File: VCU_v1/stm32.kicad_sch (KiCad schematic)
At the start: 0 parts

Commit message: added STM, broke out communications I/Os for CAN, SPI, ADC
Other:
- added sheet STM32H723ZGT6 (mcu.kicad_sch)
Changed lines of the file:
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@@
 	(generator_version "9.0")
 	(paper "A4")
+	(sheet
+		(at 114.3 64.77)
+		(size 38.1 60.96)
+		(exclude_from_sim no)
+		(in_bom yes)
+		(on_board yes)
+		(dnp no)
+		(fields_autoplaced yes)
+		(stroke
+			(width 0.1524)
+			(type solid)
+		)
+		(fill
+			(color 0 0 0 0.0000)
+		)
+		(property "Sheetname" "STM32H723ZGT6"
+			(at 114.3 64.0584 0)
+			(effects
+				(font
+					(size 1.27 1.27)
+				)
+				(justify left bottom)
+			)
+		)
+		(property "Sheetfile" "mcu.kicad_sch"
+			(at 114.3 126.3146 0)
+			(effects
+				(font
+					(size 1.27 1.27)
+				)
+				(justify left top)
+			)
+		)
+		(pin "FDCAN2_TX" input
+			(at 152.4 80.01 0)
+			(effects
+				(font
+					(size 1.27 1.27)
+				)
+				(justify right)
+			)
+		)
+		(pin "FDCAN2_RX" input
+			(at 152.4 83.82 0)
+			(effects
+				(font
+					(size 1.27 1.27)
+				)
+				(justify right)
+			)
+		)
+		(pin "SPI1_MISO" input
+			(at 152.4 102.87 0)
+			(effects
+				(font
+					(size 1.27 1.27)
+				)
+				(justify right)
+			)
+		)
+		(pin "SPI1_MOSI" input
+			(at 152.4 106.68 0)
+			(effects
+				(font
+					(size 1.27 1.27)
+				)
+				(justify right)
+			)
+		)
+		(pin "DEBUG_SWCLK" input
+			(at 114.3 68.58 180)
+			(effects
+				(font
+					(size 1.27 1.27)
+				)
+				(justify left)
+			)
+		)
+		(pin "FDCAN3_TX" input
+			(at 152.4 91.44 0)
+			(effects
+				(font
+					(size 1.27 1.27)
+				)
+				(justify right)
+			)
+		)
+		(pin "USB_D-" input
+			(at 152.4 121.92 0)
+			(effects
+				(font
+					(size 1.27 1.27)
+				)
+				(justify right)
+			)
+		)
+		(pin "DEBUG_SWO" input
+			(at 114.3 76.2 180)
+			(effects
+				(font
+					(size 1.27 1.27)
+				)
+				(justify left)
+			)
+		)
+		(pin "FDCAN1_RX" input
+			(at 152.4 72.39 0)
+			(effects
+				(font
+					(size 1.27 1.27)
+				)
+				(justify right)
+			)
+		)
+		(pin "USB_D+" input
+			(at 152.4 118.11 0)
+			(effects
+				(font
+					(size 1.27 1.27)
+				)
+				(justify right)
+			)
+		)
+		(pin "FDCAN1_TX" input
+			(at 152.4 68.58 0)
+			(effects
+				(font
+					(size 1.27 1.27)
+				)
+				(justify right)
+			)
+		)
+		(pin "DEBUG_SWDIO" input
+			(at 114.3 72.39 180)
+			(effects
+				(font
+					(size 1.27 1.27)
+				)
+				(justify left)
+			)
+		)
+		(pin "FDCAN3_RX" input
+			(at 152.4 95.25 0)
+			(effects
+				(font
+					(size 1.27 1.27)
+				)
+				(justify right)
+			)
+		)
+		(pin "I2S2-CK" input
+			(at 114.3 83.82 180)
+			(effects
+				(font
+					(size 1.27 1.27)
+				)
+				(justify left)
+			)
+		)
+		(pin "ADC3-IN9" input
+			(at 114.3 121.92 180)
+			(effects
+				(font
+					(size 1.27 1.27)
+				)
+				(justify left)
+			)
+		)
+		(pin "ADC3-IN7" input
+			(at 114.3 114.3 180)
+			(effects
+				(font
+					(size 1.27 1.27)
+				)
+				(justify left)
+			)
+		)
+		(pin "SPI1_SCK" input
+			(at 152.4 110.49 0)
+			(effects
+				(font
+					(size 1.27 1.27)
+				)
+				(justify right)
+			)
+		)
+		(pin "ADC3-IN0" input
+			(at 114.3 106.68 180)
+			(effects
+				(font
+					(size 1.27 1.27)
+				)
+				(justify left)
+			)
+		)
+		(pin "I2S2-SDO" input
+			(at 114.3 87.63 180)
+			(effects
+				(font
+					(size 1.27 1.27)
+				)
+				(justify left)
+			)
+		)
+		(pin "ADC3-IN8" input
+			(at 114.3 118.11 180)
+			(effects
+				(font
+					(size 1.27 1.27)
+				)
+				(justify left)
+			)
+		)
+		(pin "ADC3-IN6" input
+			(at 114.3 110.49 180)
+			(effects
+				(font
+					(size 1.27 1.27)
+				)
+				(justify left)
+			)
+		)
+		(pin "I2S2-WS" input
+			(at 114.3 91.44 180)
+			(effects
+				(font
+					(size 1.27 1.27)
+				)
+				(justify left)
+			)
+		)
+		(instances
+			(project "VCU_v1"
+				(path "/4ee6c2ad-9a1b-4276-b3cf-1cc8dc52967e/9e80ce31-2e03-4996-9ce1-7444f7c213d1"
+					(page "6")
+				)
+			)
+		)
+	)
 )

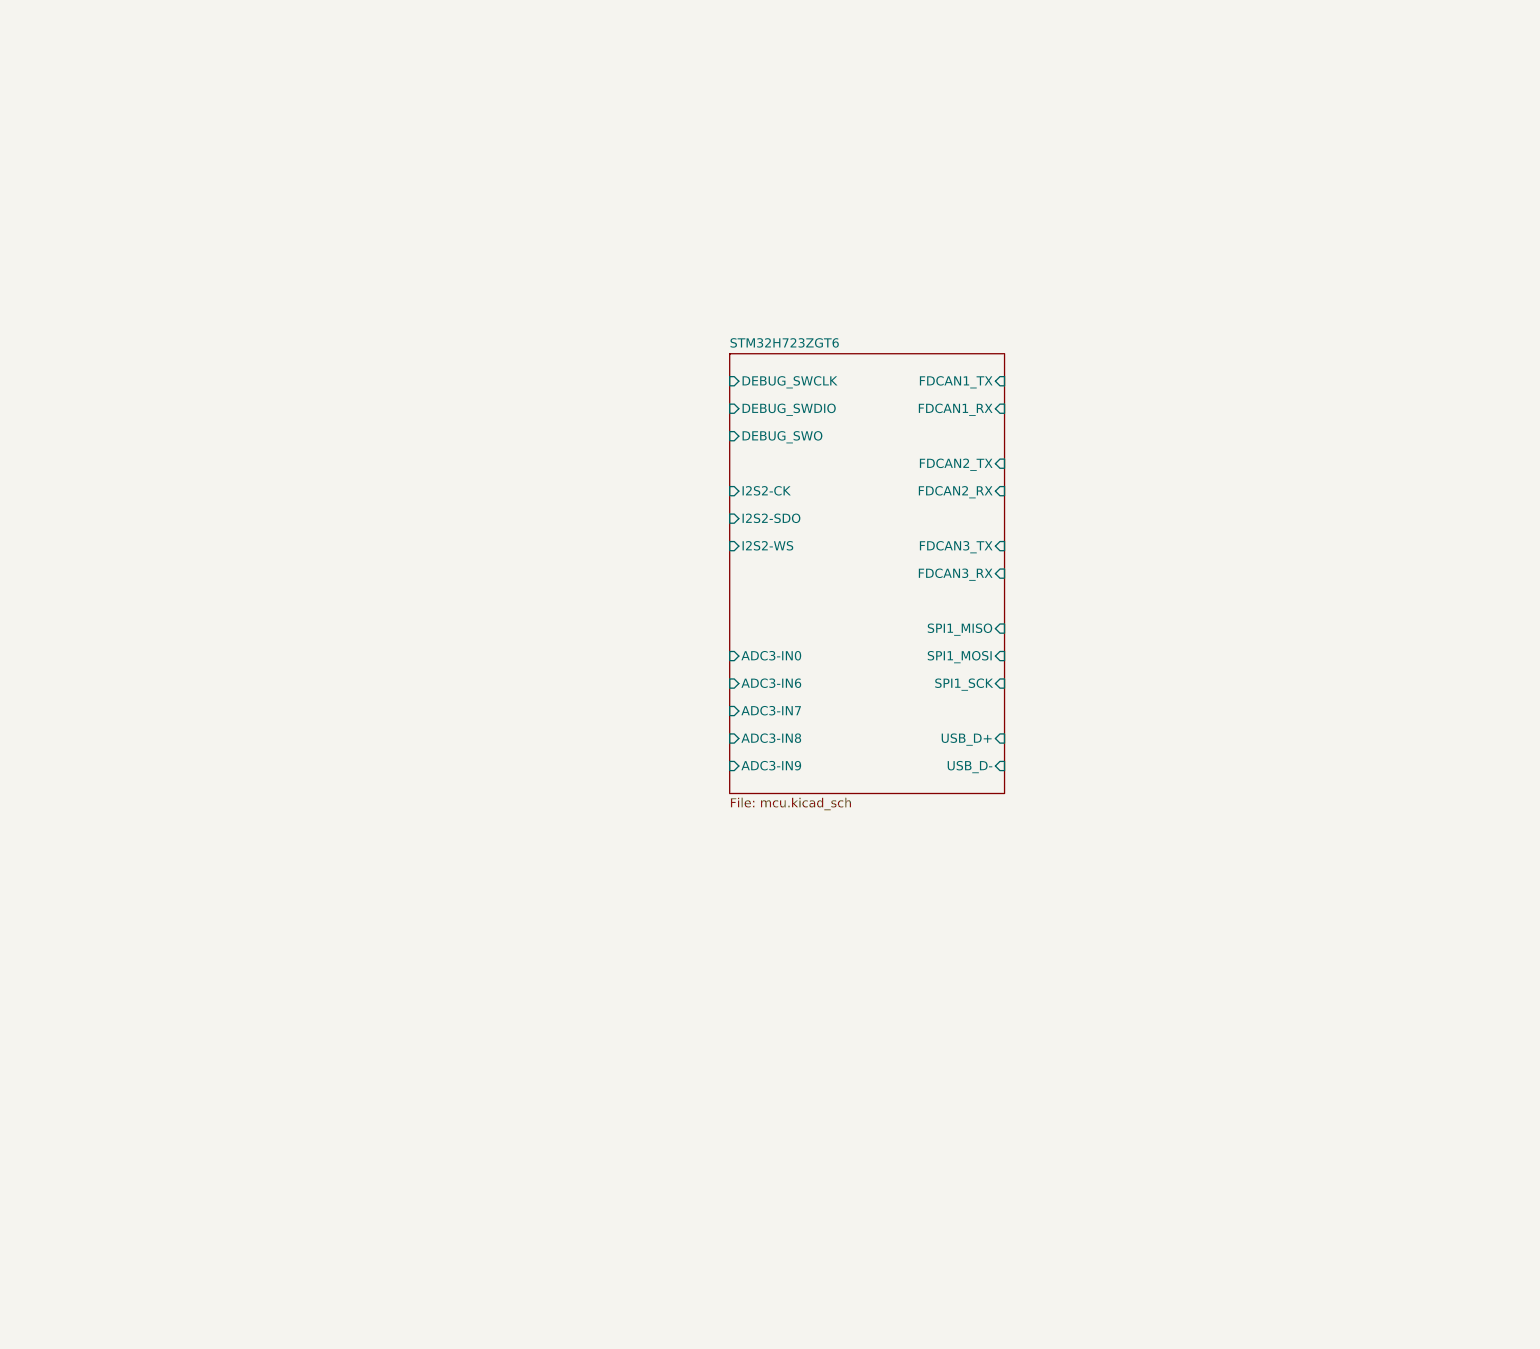
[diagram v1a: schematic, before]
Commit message: added rpp, pedal buffer/low pass, can transceivers, began connector pinout
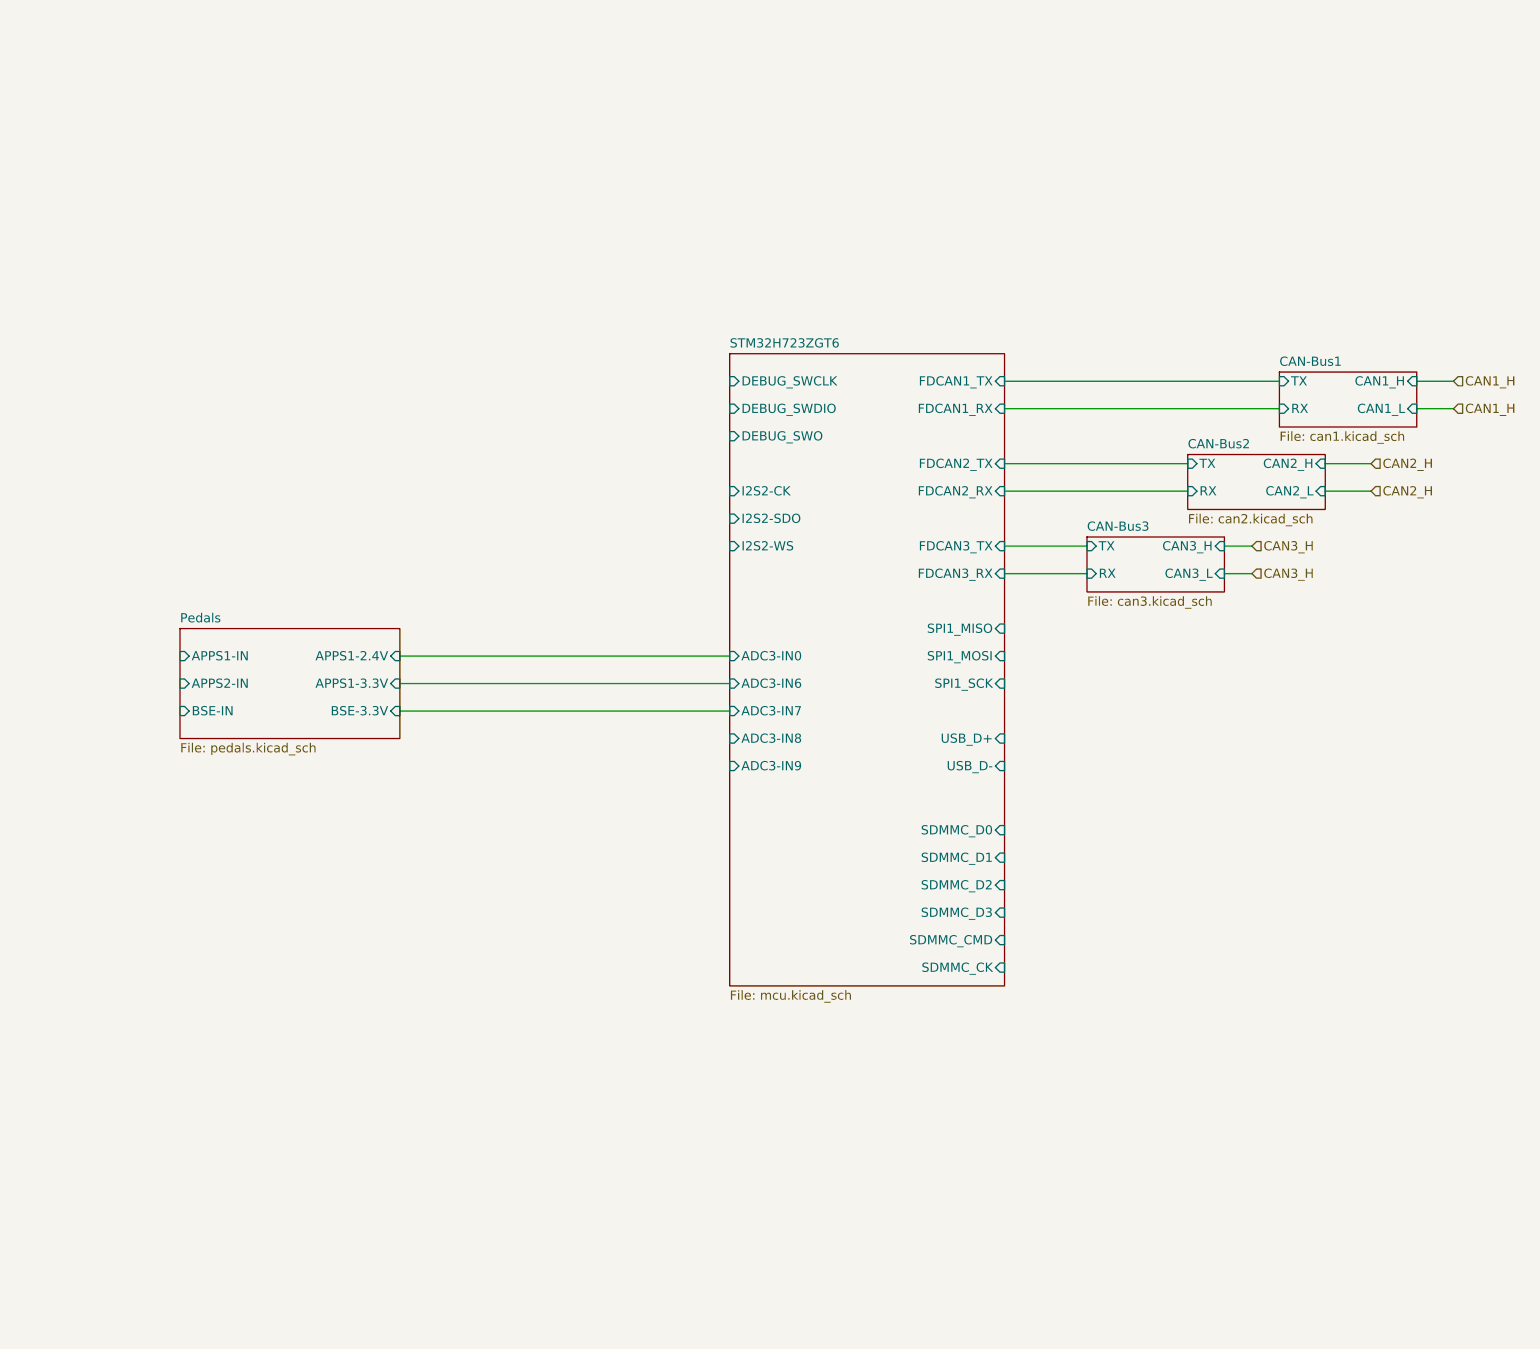
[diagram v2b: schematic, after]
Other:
- added sheet CAN-Bus1 (can1.kicad_sch)
- added sheet CAN-Bus2 (can2.kicad_sch)
- added sheet CAN-Bus3 (can3.kicad_sch)
- added sheet Pedals (pedals.kicad_sch)
- sheet STM32H723ZGT6 ports: added SDMMC_CK, SDMMC_CMD, SDMMC_D0, SDMMC_D1, SDMMC_D2, SDMMC_D3; removed none

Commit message: p dih r
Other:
- added sheet Dash+External Interface (dash_ext_int.kicad_sch)
- added sheet RTD Audio (rtd_audio.kicad_sch)
- sheet STM32H723ZGT6 ports: added GPIO_IN_E7, GPIO_IN_E8, GPIO_IN_E9, GPIO_IN_F13, GPIO_IN_F14, GPIO_IN_F15, GPIO_IN_G0, GPIO_IN_G1, GPIO_OUT_E10, GPIO_OUT_E11, GPIO_OUT_E12, GPIO_OUT_E13, GPIO_OUT_E14, GPIO_OUT_E15; removed none

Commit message: left to do before layout: wire DRS/Debug LEDs to connector, add BRUHbus ports
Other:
- sheet STM32H723ZGT6 ports: added GPIO_G10, GPIO_G11, GPIO_G12, GPIO_G13, GPIO_G14, GPIO_G15, GPIO_G2, GPIO_G3, GPIO_G4, GPIO_G5, GPIO_G6, GPIO_G7, GPIO_G8, GPIO_G9, TIM12_PWM_CH2, TIM2_PWM_CH1, TIM2_PWM_CH2, TIM2_PWM_CH3; removed none
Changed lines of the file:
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@@
 	(sheet
 		(at 113.03 40.64)
-		(size 38.1 129.54)
+		(size 38.1 157.48)
 		(exclude_from_sim no)
 		(in_bom yes)
@@
 		)
 		(property "Sheetfile" "mcu.kicad_sch"
-			(at 113.03 170.7646 0)
+			(at 113.03 198.7046 0)
 			(effects
 				(font
@@
 			)
 		)
+		(pin "GPIO_G14" input
+			(at 151.13 190.5 0)
+			(effects
+				(font
+					(size 1.27 1.27)
+				)
+				(justify right)
+			)
+		)
+		(pin "TIM2_PWM_CH1" input
+			(at 151.13 129.54 0)
+			(effects
+				(font
+					(size 1.27 1.27)
+				)
+				(justify right)
+			)
+		)
+		(pin "GPIO_G2" input
+			(at 151.13 144.78 0)
+			(effects
+				(font
+					(size 1.27 1.27)
+				)
+				(justify right)
+			)
+		)
+		(pin "GPIO_G3" input
+			(at 151.13 148.59 0)
+			(effects
+				(font
+					(size 1.27 1.27)
+				)
+				(justify right)
+			)
+		)
+		(pin "GPIO_G5" input
+			(at 151.13 156.21 0)
+			(effects
+				(font
+					(size 1.27 1.27)
+				)
+				(justify right)
+			)
+		)
+		(pin "TIM2_PWM_CH2" input
+			(at 151.13 133.35 0)
+			(effects
+				(font
+					(size 1.27 1.27)
+				)
+				(justify right)
+			)
+		)
+		(pin "GPIO_G4" input
+			(at 151.13 152.4 0)
+			(effects
+				(font
+					(size 1.27 1.27)
+				)
+				(justify right)
+			)
+		)
+		(pin "GPIO_G6" input
+			(at 151.13 160.02 0)
+			(effects
+				(font
+					(size 1.27 1.27)
+				)
+				(justify right)
+			)
+		)
+		(pin "GPIO_G8" input
+			(at 151.13 167.64 0)
+			(effects
+				(font
+					(size 1.27 1.27)
+				)
+				(justify right)
+			)
+		)
+		(pin "GPIO_G7" input
+			(at 151.13 163.83 0)
+			(effects
+				(font
+					(size 1.27 1.27)
+				)
+				(justify right)
+			)
+		)
+		(pin "GPIO_G11" input
+			(at 151.13 179.07 0)
+			(effects
+				(font
+					(size 1.27 1.27)
+				)
+				(justify right)
+			)
+		)
+		(pin "GPIO_G10" input
+			(at 151.13 175.26 0)
+			(effects
+				(font
+					(size 1.27 1.27)
+				)
+				(justify right)
+			)
+		)
+		(pin "GPIO_G9" input
+			(at 151.13 171.45 0)
+			(effects
+				(font
+					(size 1.27 1.27)
+				)
+				(justify right)
+			)
+		)
+		(pin "GPIO_G12" input
+			(at 151.13 182.88 0)
+			(effects
+				(font
+					(size 1.27 1.27)
+				)
+				(justify right)
+			)
+		)
+		(pin "GPIO_G15" input
+			(at 151.13 194.31 0)
+			(effects
+				(font
+					(size 1.27 1.27)
+				)
+				(justify right)
+			)
+		)
+		(pin "GPIO_G13" input
+			(at 151.13 186.69 0)
+			(effects
+				(font
+					(size 1.27 1.27)
+				)
+				(justify right)
+			)
+		)
+		(pin "TIM12_PWM_CH2" input
+			(at 151.13 140.97 0)
+			(effects
+				(font
+					(size 1.27 1.27)
+				)
+				(justify right)
+			)
+		)
+		(pin "TIM2_PWM_CH3" input
+			(at 151.13 137.16 0)
+			(effects
+				(font
+					(size 1.27 1.27)
+				)
+				(justify right)
+			)
+		)
